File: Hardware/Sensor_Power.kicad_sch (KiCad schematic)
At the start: 46 parts, among them IC2 TPS61089RNRR, IC3 AP2205-W5-7, IC4 AP2205-W5-7, IC5 TPS61089RNRR

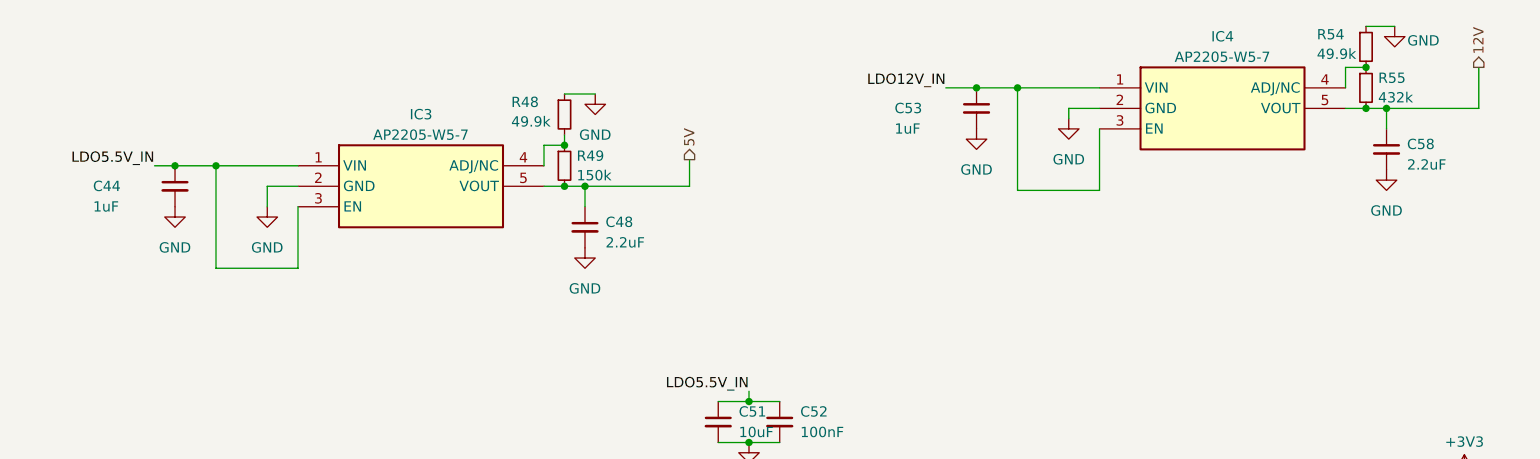
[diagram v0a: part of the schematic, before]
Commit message: schematic changes and updated tvs footprints
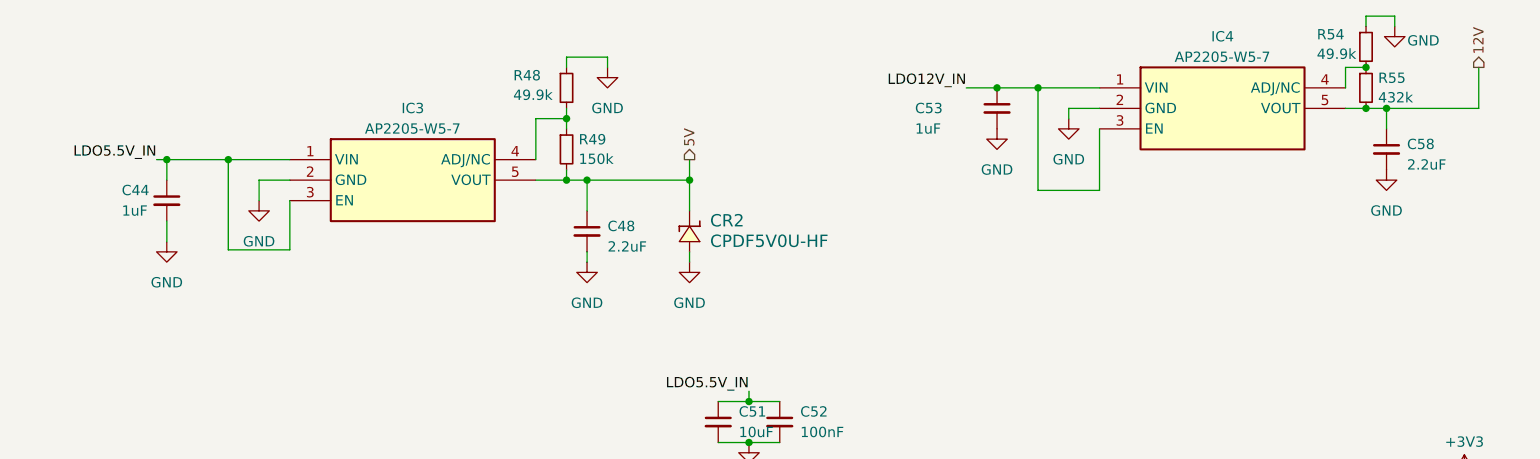
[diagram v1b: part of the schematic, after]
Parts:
- added CR2: CPDF5V0U-HF, iclr:CPD, symbol iclr:CPDF5V0U-HF
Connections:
- net 5V: now also CR2.2
- net GND: now also CR2.1
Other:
- moved on the sheet: C44, C48, C53, IC3, R48, R49
